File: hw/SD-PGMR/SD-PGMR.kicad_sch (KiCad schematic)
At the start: 45 parts, among them J1 CONN_01x07 Socket, J2 Conn_01x03 HDR, J3 J-V3.3, J4 Conn_01x03 HDR, Q1 MMBT3906, Q2 MMBT3904, Q3 DMG2305UX, SW1 SW PB-MOM, SW2 SW PB-MOM, U1 74HCT574, U10 SST39SF0n0, U2 74LCX574, U3 AES-Pico, U4 74HCT138, U5 74HCT191, U6 74HCT191, U7 74HCT191, U8 74HCT191, U9 74HCT191

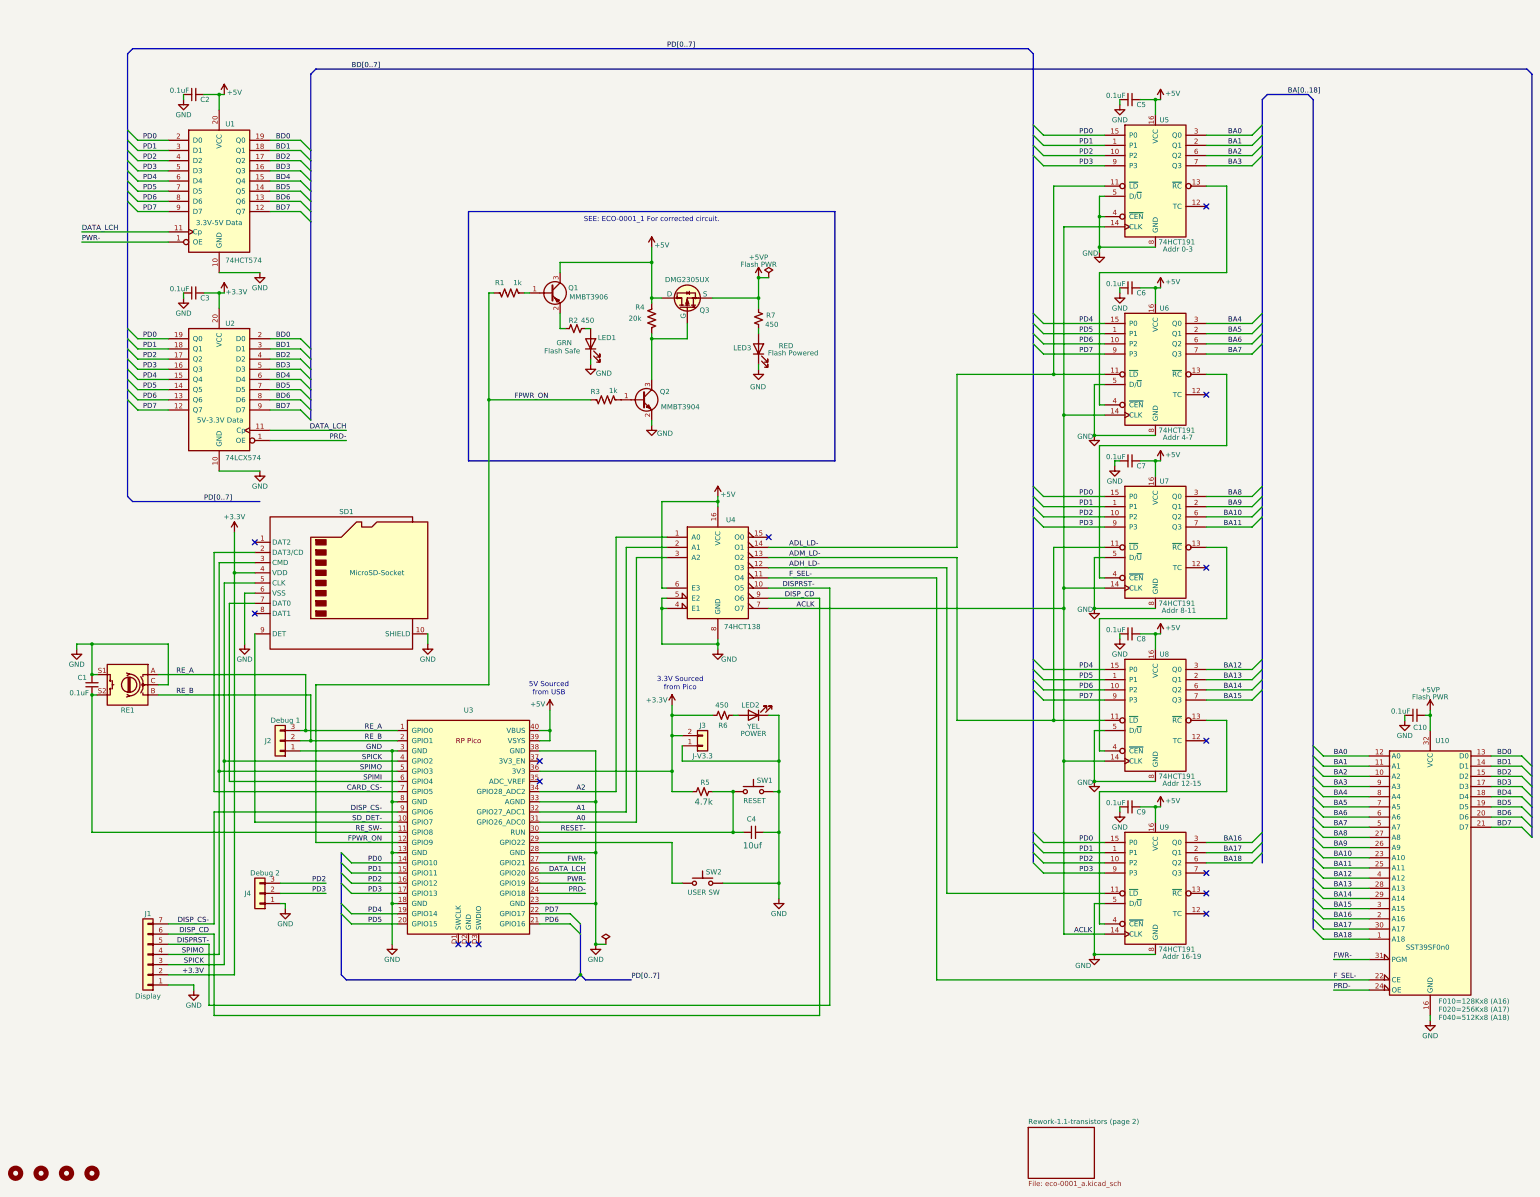
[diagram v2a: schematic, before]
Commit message: Re-design and re-layout with new power circuit
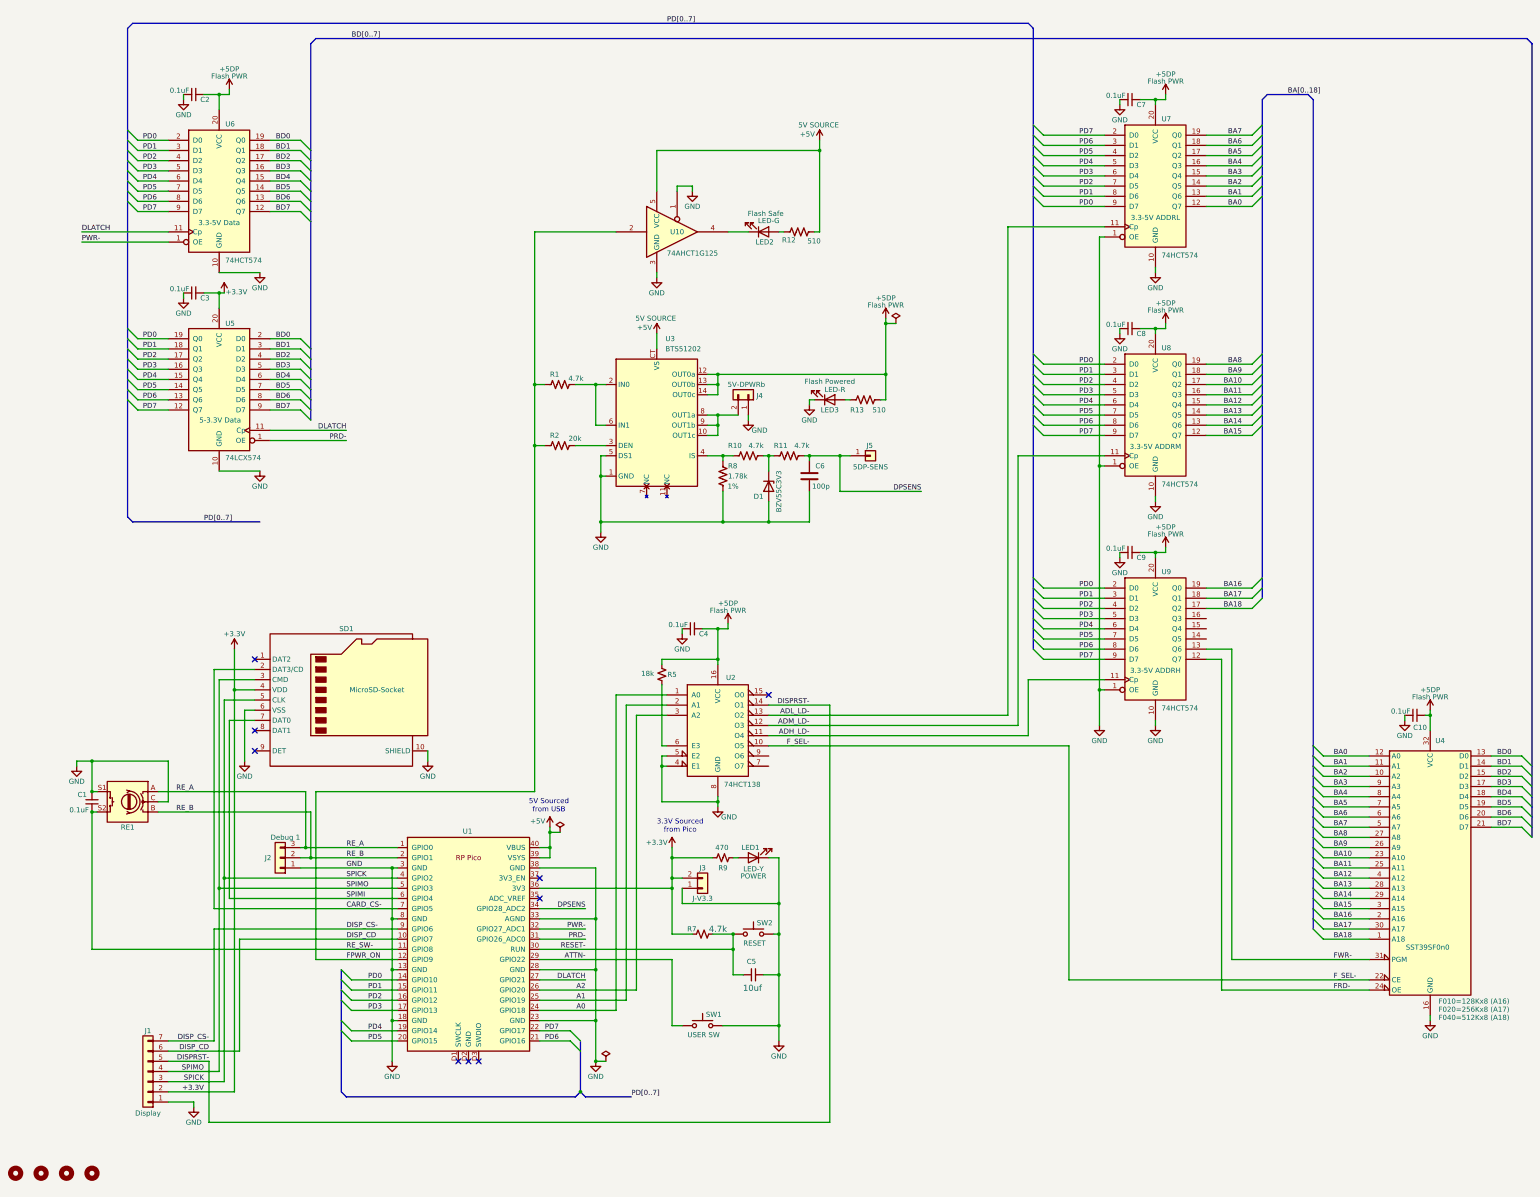
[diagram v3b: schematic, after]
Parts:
- removed C5, C6: 0.1uF, Capacitor_SMD:C_0603_1608Metric_Pad1.08x0.95mm_HandSolder, symbol Device:C_Small
- removed J4: Conn_01x03 HDR, Connector_PinHeader_2.54mm:PinHeader_1x03_P2.54mm_Vertical, symbol Connector_Generic:Conn_01x03
- removed LED1: GRN, LED_THT:LED_D5.0mm, symbol Device:LED
- removed Q1: MMBT3906, Package_TO_SOT_SMD:SOT-23, symbol Transistor_BJT:BC807
- removed Q2: MMBT3904, Package_TO_SOT_SMD:SOT-23, symbol Transistor_BJT:MMBT3904
- removed Q3: DMG2305UX, Package_TO_SOT_SMD:SOT-23, symbol AES_Library:DMG2305UX-AES
- removed R2, R7: 450, Resistor_SMD:R_0805_2012Metric_Pad1.20x1.40mm_HandSolder, symbol Device:R_Small_US
- removed R3: 1k, Resistor_SMD:R_0805_2012Metric_Pad1.20x1.40mm_HandSolder, symbol Device:R_US
- removed R4: 20k, Resistor_SMD:R_0805_2012Metric_Pad1.20x1.40mm_HandSolder, symbol Device:R_US
- removed U5, U6, U7, U8, U9: 74HCT191, Package_SO:SOIC-16_3.9x9.9mm_P1.27mm, symbol AES_Library:74HCT191-AES
- added C6: 100p, Capacitor_SMD:C_0603_1608Metric_Pad1.08x0.95mm_HandSolder, symbol Device:C
- added C9: 0.1uF, Capacitor_SMD:C_0603_1608Metric_Pad1.08x0.95mm_HandSolder, symbol Device:C_Small
- added D1: BZV55C3V3, Diode_SMD:D_MiniMELF, symbol Diode:BZV55C3V3
- added J4: CONN 1x2 HDR, Connector_PinHeader_2.54mm:PinHeader_1x02_P2.54mm_Vertical, symbol Connector_Generic:Conn_01x02
- added J5: HDR 1x1 Pin, Connector_PinHeader_2.54mm:PinHeader_1x01_P2.54mm_Vertical, symbol Connector_Generic:Conn_01x01
- added LED2: LED-G, LED_THT:LED_D5.0mm, symbol Device:LED
- added R10, R11: 4.7k, Resistor_SMD:R_0805_2012Metric_Pad1.20x1.40mm_HandSolder, symbol Device:R_US
- added R12, R13: 510, Resistor_SMD:R_0805_2012Metric_Pad1.20x1.40mm_HandSolder, symbol Device:R_US
- added R2: 20k, Resistor_SMD:R_0805_2012Metric_Pad1.20x1.40mm_HandSolder, symbol Device:R_US
- added R5: 18k, Resistor_SMD:R_0805_2012Metric_Pad1.20x1.40mm_HandSolder, symbol Device:R_Small_US
- added R8: 1.78k, Resistor_SMD:R_0805_2012Metric_Pad1.20x1.40mm_HandSolder, symbol Device:R_US
- added U10: 74AHCT1G125, Package_TO_SOT_SMD:SOT-23-5_HandSoldering, symbol 74xGxx:74AHCT1G125
- added U3: BTS51202, AES_Library:AES-Inf-BTS5120-DSOP14-BP, symbol AES_Library:AES-BTS5120-2-2CH_PWR_SW
- added U7, U8, U9: 74HCT574, Package_SO:SOIC-20W_7.5x12.8mm_P1.27mm, symbol 74xx:74HCT574
- LED1: renamed from LED2; value YEL -> LED-Y
- LED3: value RED -> LED-R; now in the parts list
- R1: value 1k -> 4.7k; now in the parts list
- R9: renamed from R6; value 450 -> 470
- U5: renamed from U2; Function 5V-3.3V Data -> 5-3.3V Data
- U6: renamed from U1; Function 3.3V-5V Data -> 3.3-5V Data
- renumbered C9 to C4, C4 to C5, R5 to R7, SW2 to SW1, SW1 to SW2, U3 to U1, U4 to U2, U10 to U4
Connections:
- net +5V: now also R12.1, U10.5 (VCC), U3.CT (VS); no longer C2.2, C4.2, C7.2, C8.2, U2.16 (VCC), U2.6 (E3), U6.20 (VCC)
- net A0: now also U1.24 (GPIO18), U2.1 (A0); no longer U1.31 (GPIO26_ADC0), U2.3 (A2)
- net A1: now also U1.25 (GPIO19); no longer U1.32 (GPIO27_ADC1)
- net A2: now also U1.26 (GPIO20), U2.3 (A2); no longer U1.34 (GPIO28_ADC2), U2.1 (A0)
- net ADH_LD-: now also U2.11 (O4), U9.11 (Cp); no longer U2.12 (O3)
- net ADL_LD-: now also U2.13 (O2), U7.11 (Cp); no longer U2.14 (O1)
- net ADM_LD-: now also U2.12 (O3), U8.11 (Cp); no longer U2.13 (O2)
- net BA0: now also U7.12 (Q7)
- net BA1: now also U7.13 (Q6)
- net BA10: now also U8.17 (Q2)
- net BA11: now also U8.16 (Q3)
- net BA12: now also U8.15 (Q4)
- net BA13: now also U8.14 (Q5)
- net BA14: now also U8.13 (Q6)
- net BA15: now also U8.12 (Q7)
- net BA16: now also U9.19 (Q0)
- net BA17: now also U9.18 (Q1)
- net BA18: now also U9.17 (Q2)
- net BA2: now also U7.14 (Q5)
- net BA3: now also U7.15 (Q4)
- net BA4: now also U7.16 (Q3)
- net BA5: now also U7.17 (Q2)
- net BA6: now also U7.18 (Q1)
- net BA7: now also U7.19 (Q0)
- net BA8: now also U8.19 (Q0)
- net BA9: now also U8.18 (Q1)
- net DISPRST-: now also U2.14 (O1); no longer U2.10 (O5)
- net DISP_CD: now also U1.10 (GPIO7); no longer U2.9 (O6)
- net FPWR_ON: now also R2.1, U10.2
- net FWR-: now also U9.13 (Q6); no longer U1.27 (GPIO21)
- net F_SEL-: now also U2.10 (O5); no longer U2.11 (O4)
- net GND: now also C6.1, C9.1, D1.2 (A), J4.1 (Pin_1), R8.2, U10.1, U10.3 (GND), U3.1 (GND), U3.5 (DS1), U7.1 (OE), U7.10 (GND), U8.1 (OE), U8.10 (GND), U9.1 (OE), U9.10 (GND)
- net PD0: now also U7.9 (D7), U8.2 (D0), U9.2 (D0)
- net PD1: now also U7.8 (D6), U8.3 (D1), U9.3 (D1)
- net PD2: now also U7.7 (D5), U8.4 (D2), U9.4 (D2)
- net PD3: now also U7.6 (D4), U8.5 (D3), U9.5 (D3)
- net PD4: now also U7.5 (D3), U8.6 (D4), U9.6 (D4)
- net PD5: now also U7.4 (D2), U8.7 (D5), U9.7 (D5)
- net PD6: now also U7.3 (D1), U8.8 (D6), U9.8 (D6)
- net PD7: now also U7.2 (D0), U8.9 (D7), U9.9 (D7)
- net PRD-: now also U1.31 (GPIO26_ADC0); no longer U1.24 (GPIO18), U4.24 (OE)
- net PWR-: now also U1.32 (GPIO27_ADC1); no longer U1.25 (GPIO19)
- net at R1.2: now also U3.2 (IN0), U3.6 (IN1)
- net ATTN-: now reaches SW1.1, U1.29 (GPIO22)
- net at LED3.2 (A): now also R13.1
- net +5VP renamed +5DP
- net +5DP: now also C2.2, C4.2, C7.2, C8.2, U2.16 (VCC), U6.20 (VCC), C9.2, R13.2, R5.2, U3.12 (OUT0a), U3.13 (OUT0b), U3.14 (OUT0c), U7.20 (VCC), U8.20 (VCC), U9.20 (VCC)
- net ACLK: no longer names the net of U2.7 (O7)
- net DATA_LCH renamed DLATCH
- net DLATCH: now also U1.27 (GPIO21); no longer U1.26 (GPIO20)
- net SD_DET-: no longer names the net of SD1.9 (DET)
- net SD_DET-: no longer U1.10 (GPIO7)
- new net: LED2.1 (K), U10.4
- new net: LED2.2 (A), R12.2
- new net: R10.1, R8.1, U3.4 (IS)
- new net: D1.1 (K), R10.2, R11.1
- new net: J4.2 (Pin_2), U3.10 (OUT1c), U3.8 (OUT1a), U3.9 (OUT1b)
- new net: R5.1, U2.6 (E3)
- new net: R2.2, U3.3 (DEN)
- new net DPSENS: C6.2, J5.1 (Pin_1), R11.2, U1.34 (GPIO28_ADC2)
- new net FRD-: U4.24 (OE), U9.12 (Q7)
- no-connect marks 15 -> 9
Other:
- removed sheet Rework-1.1-transistors (page 2)
- note removed: "SEE: ECO-0001_1 For corrected circuit."
- moved on the sheet: C1, C4, C5, J1, J2, J3, LED1, R7, R9, RE1, SD1, SW1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
